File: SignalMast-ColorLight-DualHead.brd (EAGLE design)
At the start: 12.7 x 36.3 mm, 8 parts

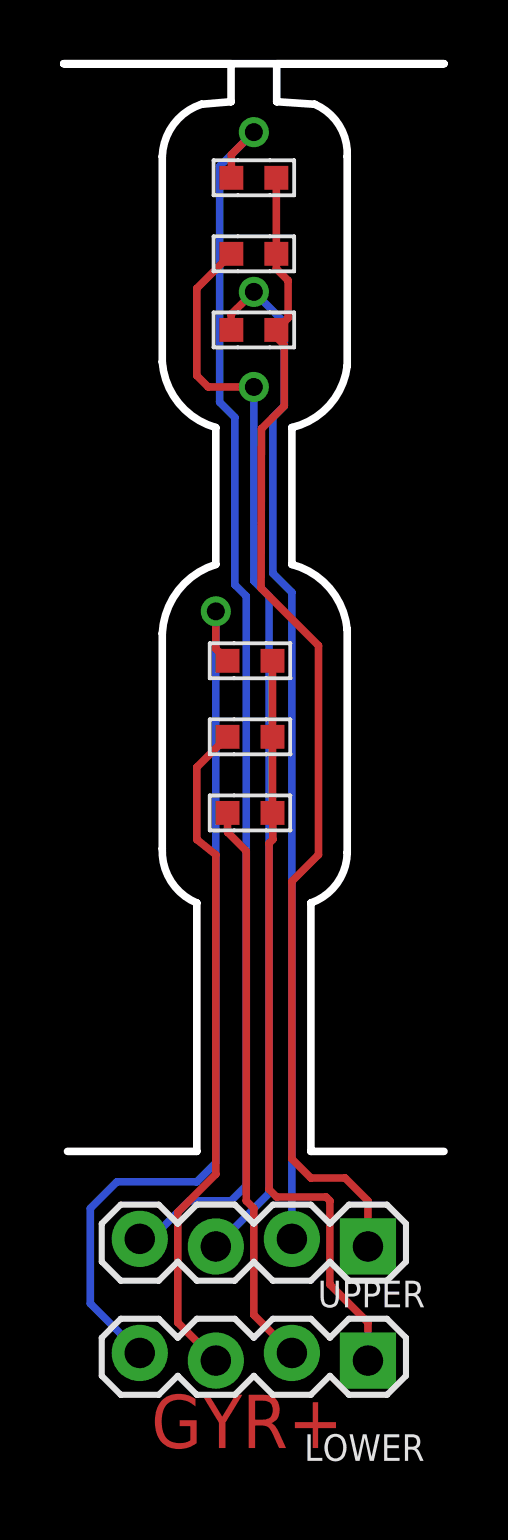
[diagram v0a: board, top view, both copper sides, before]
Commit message: normalized values
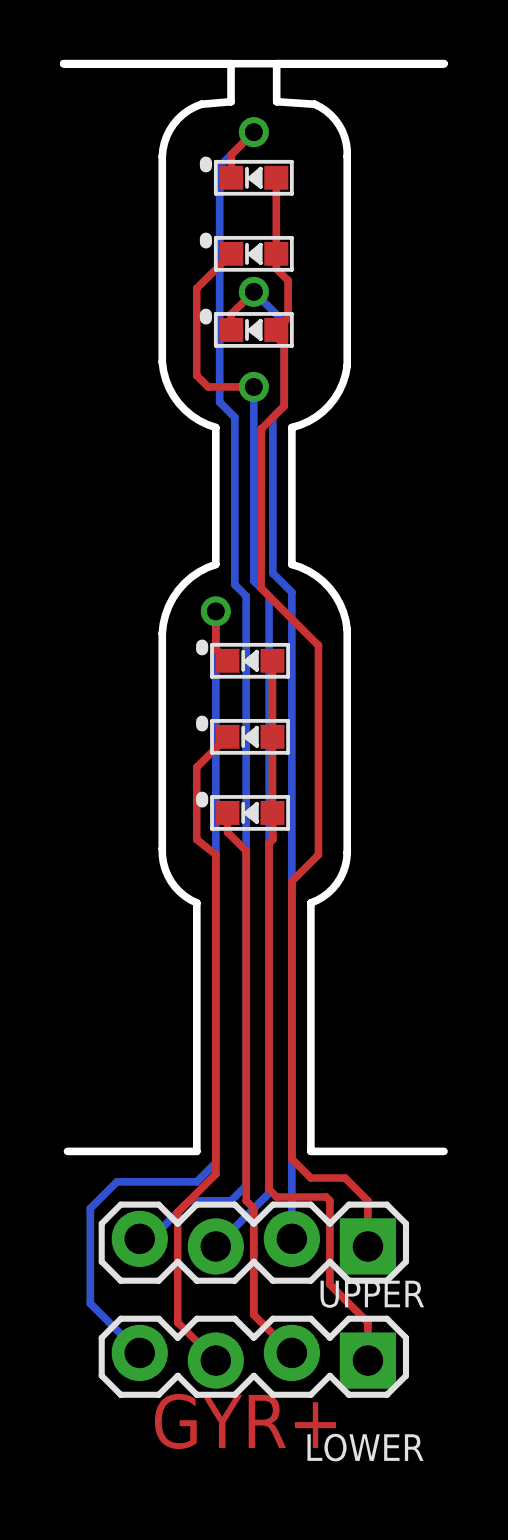
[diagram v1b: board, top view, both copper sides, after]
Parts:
- LOWER, UPPER: value 1x4 0.100 -> 0.100
- turned LED1 to 0 degrees
- turned LED2 to 0 degrees
- turned LED3 to 0 degrees
- turned LED4 to 0 degrees
- turned LED5 to 0 degrees
- turned LED6 to 0 degrees
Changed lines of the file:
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@@
 </autorouter>
 <elements>
-<element name="UPPER" library="SPCoast" package="1X04_LOCK" value="1x4 0.100" x="10.16" y="7.62" smashed="yes" rot="R180">
+<element name="UPPER" library="SPCoast" package="1X04_LOCK" value="0.100" x="10.16" y="7.62" smashed="yes" rot="R180">
 <attribute name="NAME" x="12.065" y="6.35" size="0.889" layer="25" font="vector" ratio="11" rot="R180"/>
 </element>
-<element name="LOWER" library="SPCoast" package="1X04_LOCK" value="1x4 0.100" x="10.16" y="3.81" smashed="yes" rot="R180">
+<element name="LOWER" library="SPCoast" package="1X04_LOCK" value="0.100" x="10.16" y="3.81" smashed="yes" rot="R180">
 <attribute name="NAME" x="12.049" y="1.222" size="0.889" layer="25" font="vector" ratio="11" rot="R180"/>
 </element>
-<element name="LED1" library="SPCoast" package="0603-LED" value="R" x="6.35" y="38.1" smashed="yes" rot="R180">
-<attribute name="OPL" value="19-217-R6C-AL1M2VY-3T" x="6.35" y="38.1" size="1.778" layer="27" rot="R180" display="off"/>
-<attribute name="VALUE" x="11.43" y="38.735" size="1.27" layer="27" font="vector" rot="R180"/>
+<element name="LED1" library="SPCoast" package="0603-LED" value="R" x="6.35" y="38.1" smashed="yes">
+<attribute name="OPL" value="19-217-R6C-AL1M2VY-3T" x="6.35" y="38.1" size="1.778" layer="27" display="off"/>
+<attribute name="VALUE" x="1.27" y="37.465" size="1.27" layer="27" font="vector"/>
 </element>
-<element name="LED2" library="SPCoast" package="0603-LED" value="Y" x="6.35" y="40.64" smashed="yes" rot="R180">
-<attribute name="OPL" value="19-217-Y5C-AM1N1VY-3T" x="6.35" y="40.64" size="1.778" layer="27" rot="R180" display="off"/>
-<attribute name="VALUE" x="11.43" y="41.275" size="1.27" layer="27" font="vector" rot="R180"/>
+<element name="LED2" library="SPCoast" package="0603-LED" value="Y" x="6.35" y="40.64" smashed="yes">
+<attribute name="OPL" value="19-217-Y5C-AM1N1VY-3T" x="6.35" y="40.64" size="1.778" layer="27" display="off"/>
+<attribute name="VALUE" x="1.27" y="40.005" size="1.27" layer="27" font="vector"/>
 </element>
-<element name="LED3" library="SPCoast" package="0603-LED" value="G" x="6.35" y="43.18" smashed="yes" rot="R180">
-<attribute name="OPL" value="19-217-G7C-AN1P2-3T " x="6.35" y="43.18" size="1.778" layer="27" rot="R180" display="off"/>
-<attribute name="VALUE" x="11.43" y="43.815" size="1.27" layer="27" font="vector" rot="R180"/>
+<element name="LED3" library="SPCoast" package="0603-LED" value="G" x="6.35" y="43.18" smashed="yes">
+<attribute name="OPL" value="19-217-G7C-AN1P2-3T " x="6.35" y="43.18" size="1.778" layer="27" display="off"/>
+<attribute name="VALUE" x="1.27" y="42.545" size="1.27" layer="27" font="vector"/>
 </element>
-<element name="LED4" library="SPCoast" package="0603-LED" value="R" x="6.223" y="21.971" smashed="yes" rot="R180">
-<attribute name="OPL" value="19-217-R6C-AL1M2VY-3T" x="6.223" y="21.971" size="1.778" layer="27" rot="R180" display="off"/>
-<attribute name="VALUE" x="11.303" y="22.606" size="1.27" layer="27" font="vector" rot="R180"/>
+<element name="LED4" library="SPCoast" package="0603-LED" value="R" x="6.223" y="21.971" smashed="yes">
+<attribute name="OPL" value="19-217-R6C-AL1M2VY-3T" x="6.223" y="21.971" size="1.778" layer="27" display="off"/>
+<attribute name="VALUE" x="1.143" y="21.336" size="1.27" layer="27" font="vector"/>
 </element>
-<element name="LED5" library="SPCoast" package="0603-LED" value="Y" x="6.223" y="24.511" smashed="yes" rot="R180">
-<attribute name="OPL" value="19-217-Y5C-AM1N1VY-3T" x="6.223" y="24.511" size="1.778" layer="27" rot="R180" display="off"/>
-<attribute name="VALUE" x="11.303" y="25.146" size="1.27" layer="27" font="vector" rot="R180"/>
+<element name="LED5" library="SPCoast" package="0603-LED" value="Y" x="6.223" y="24.511" smashed="yes">
+<attribute name="OPL" value="19-217-Y5C-AM1N1VY-3T" x="6.223" y="24.511" size="1.778" layer="27" display="off"/>
+<attribute name="VALUE" x="1.143" y="23.876" size="1.27" layer="27" font="vector"/>
 </element>
-<element name="LED6" library="SPCoast" package="0603-LED" value="G" x="6.223" y="27.051" smashed="yes" rot="R180">
-<attribute name="OPL" value="19-217-G7C-AN1P2-3T " x="6.223" y="27.051" size="1.778" layer="27" rot="R180" display="off"/>
-<attribute name="VALUE" x="11.303" y="27.686" size="1.27" layer="27" font="vector" rot="R180"/>
+<element name="LED6" library="SPCoast" package="0603-LED" value="G" x="6.223" y="27.051" smashed="yes">
+<attribute name="OPL" value="19-217-G7C-AN1P2-3T " x="6.223" y="27.051" size="1.778" layer="27" display="off"/>
+<attribute name="VALUE" x="1.143" y="26.416" size="1.27" layer="27" font="vector"/>
 </element>
 </elements>
